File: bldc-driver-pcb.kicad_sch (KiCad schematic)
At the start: 0 parts

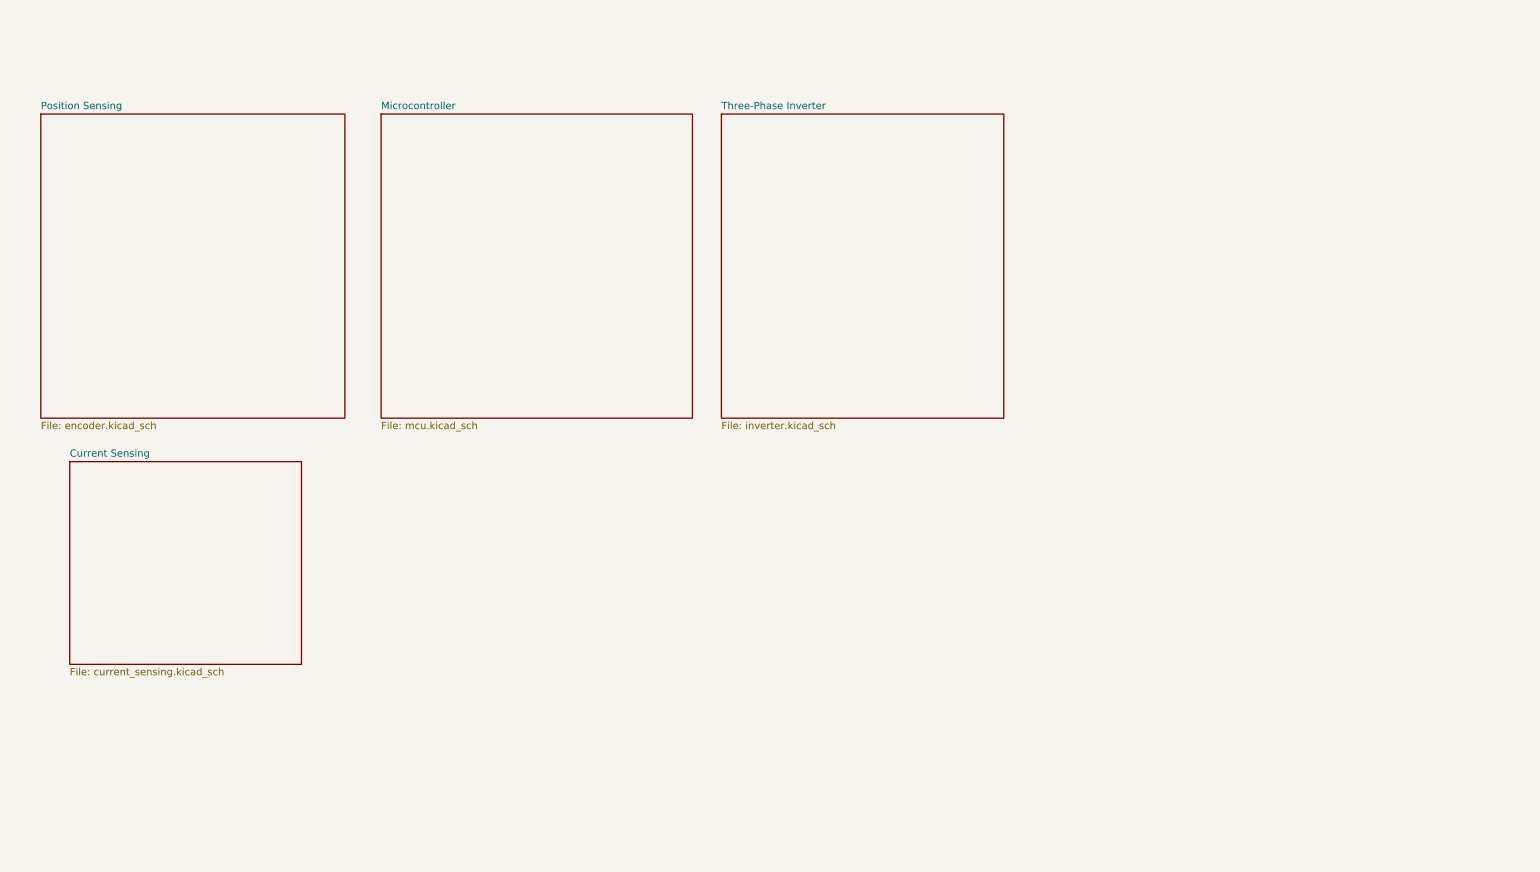
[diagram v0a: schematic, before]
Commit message: Add MCU stuff, cortex debug connector and docs
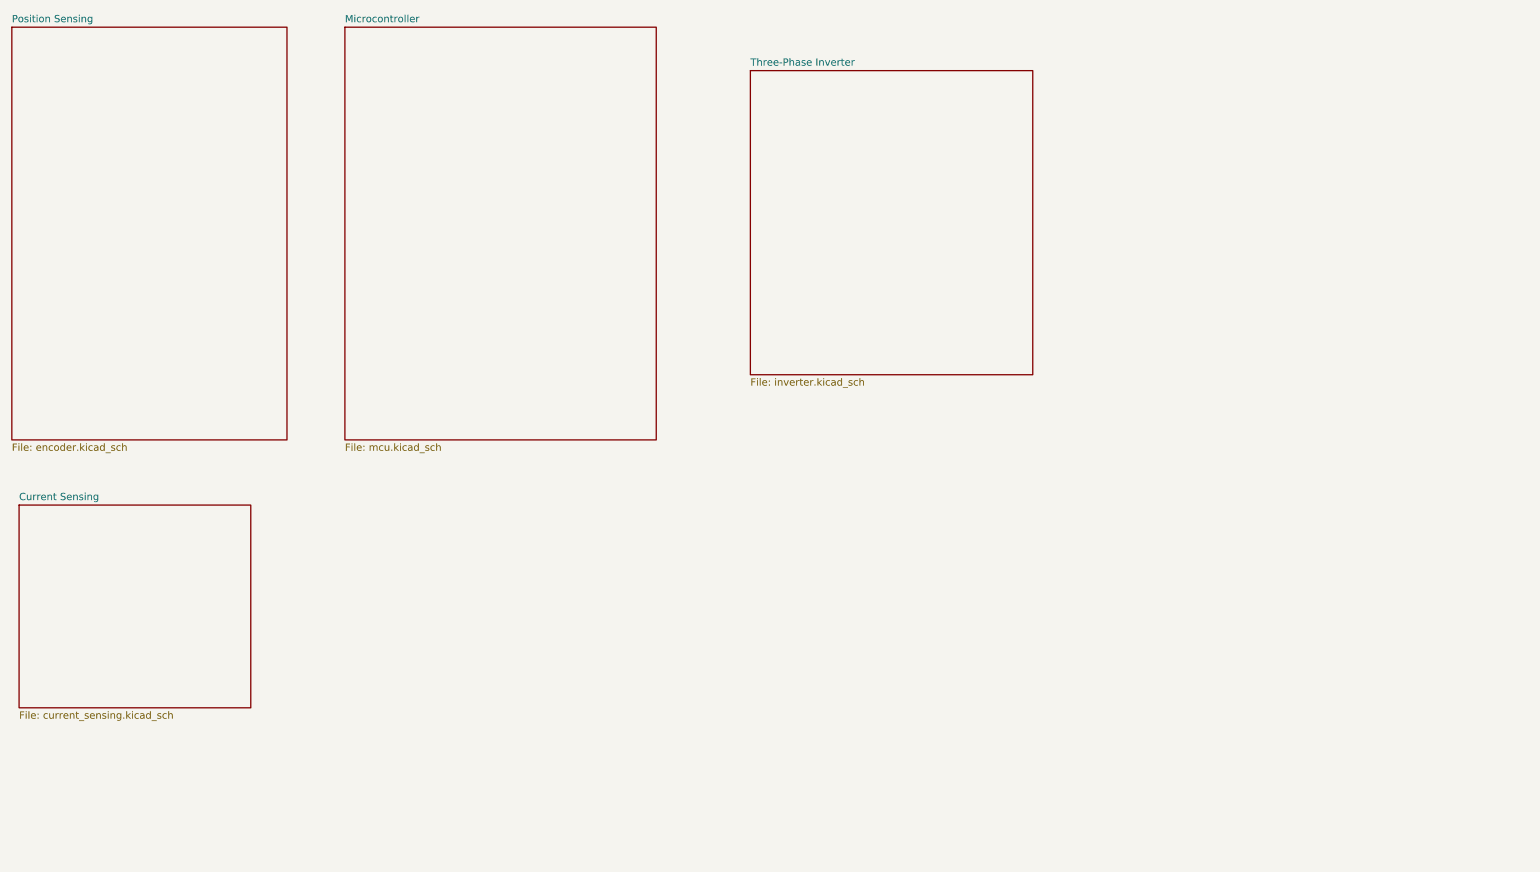
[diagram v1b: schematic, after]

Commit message: Initial routing
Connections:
- no-connect marks 0 -> 9
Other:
- sheet Current Sensing ports: added CSA_1_IN+, CSA_1_IN-, CSA_1_VOUT, CSA_2_IN+, CSA_2_IN-, CSA_2_VOUT, CSA_3_IN+, CSA_3_IN-, CSA_3_VOUT, OPAMP_VCC, VREF_1, VREF_2, VREF_3; removed none
- sheet Microcontroller ports: added 3V3_MCU, ADC_AIN2, ADC_AIN3, ADC_AIN4, ADC_VREFA, ENCODER_CSn, SERCOM1_PAD0, SERCOM1_PAD1, SERCOM1_PAD2, SERCOM1_PAD3, TCC0_WO0, TCC0_WO1, TCC0_WO2, TCC0_WO3, TCC0_WO4, TCC0_WO5, TCC0_WO6, TCC0_WO7; removed none
- sheet Position Sensing ports: added ENCODER_3V3, ENCODER_CSn, ENCODER_MISO, ENCODER_MOSI, ENCODER_SCLK; removed none
- sheet Three-Phase Inverter ports: added CSA_1_IN+, CSA_1_IN-, CSA_2_IN+, CSA_2_IN-, CSA_3_IN+, CSA_3_IN-, HALF_BRIDGE_1_HI, HALF_BRIDGE_1_LO, HALF_BRIDGE_1_OUT, HALF_BRIDGE_2_HI, HALF_BRIDGE_2_LO, HALF_BRIDGE_2_OUT, HALF_BRIDGE_3_HI, HALF_BRIDGE_3_LO, HALF_BRIDGE_3_OUT; removed none

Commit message: More routing
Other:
- sheet Microcontroller ports: added DBG_LED_GREEN, DBG_LED_RED, DRV8316_CSn, RESET, SERCOM3_PAD0, SERCOM3_PAD1, SERCOM5_PAD2, SERCOM5_PAD3, SWCLK, SWDIO, USB_D+, USB_D-, VDDANA, VDDCORE, VDDIN, VDDIO, XIN, XIN32, XOUT, XOUT32; removed none

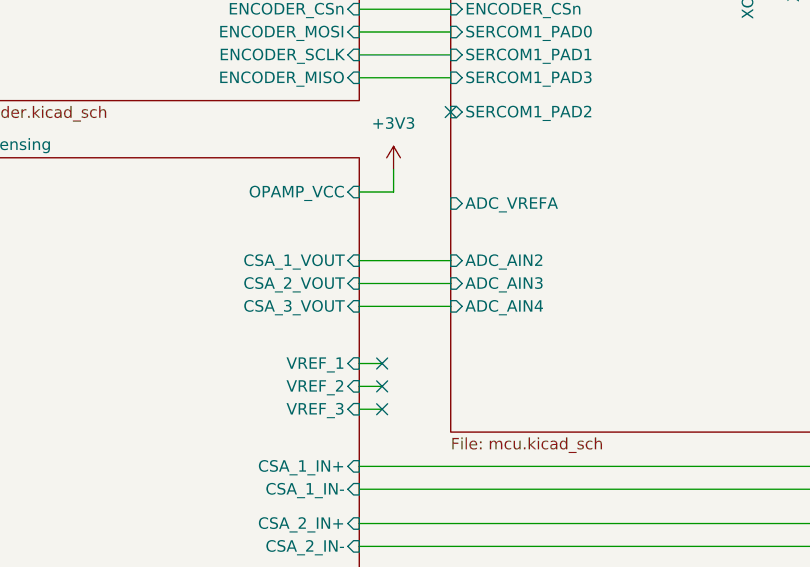
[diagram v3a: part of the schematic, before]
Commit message: Reroute everything
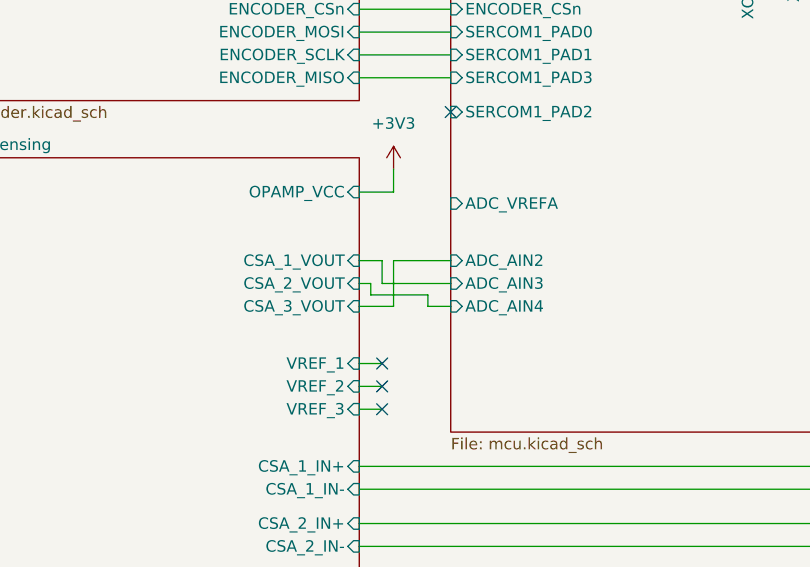
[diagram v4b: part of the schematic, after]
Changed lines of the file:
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@@
+	(wire
+		(pts
+			(xy 102.87 60.96) (xy 105.41 60.96)
+		)
+		(stroke
+			(width 0)
+			(type default)
+		)
+	)
 	(wire
 		(pts
@@
 	(wire
 		(pts
+			(xy 97.79 58.42) (xy 105.41 58.42)
+		)
+		(stroke
+			(width 0)
+			(type default)
+		)
+	)
+	(wire
+		(pts
+			(xy 95.25 58.42) (xy 96.52 58.42)
+		)
+		(stroke
+			(width 0)
+			(type default)
+		)
+	)
+	(wire
+		(pts
 			(xy 99.06 48.26) (xy 99.06 45.72)
 		)
@@
 	(wire
 		(pts
-			(xy 95.25 58.42) (xy 105.41 58.42)
+			(xy 99.06 55.88) (xy 105.41 55.88)
+		)
+		(stroke
+			(width 0)
+			(type default)
+		)
+	)
+	(wire
+		(pts
+			(xy 99.06 60.96) (xy 99.06 55.88)
 		)
 		(stroke
@@
 	(wire
 		(pts
+			(xy 97.79 55.88) (xy 97.79 58.42)
+		)
+		(stroke
+			(width 0)
+			(type default)
+		)
+	)
+	(wire
+		(pts
 			(xy 95.25 93.98) (xy 186.69 93.98)
 		)
@@
 	(wire
 		(pts
+			(xy 95.25 60.96) (xy 99.06 60.96)
+		)
+		(stroke
+			(width 0)
+			(type default)
+		)
+	)
+	(wire
+		(pts
 			(xy 95.25 48.26) (xy 99.06 48.26)
 		)
@@
 	(wire
 		(pts
-			(xy 95.25 55.88) (xy 105.41 55.88)
+			(xy 96.52 58.42) (xy 96.52 59.69)
 		)
 		(stroke
@@
 	(wire
 		(pts
+			(xy 96.52 59.69) (xy 102.87 59.69)
+		)
+		(stroke
+			(width 0)
+			(type default)
+		)
+	)
+	(wire
+		(pts
 			(xy 175.26 44.45) (xy 186.69 44.45)
 		)
@@
 	(wire
 		(pts
-			(xy 95.25 60.96) (xy 105.41 60.96)
-		)
-		(stroke
-			(width 0)
-			(type default)
-		)
-	)
-	(wire
-		(pts
 			(xy 175.26 41.91) (xy 186.69 41.91)
 		)
@@
 	(wire
 		(pts
+			(xy 95.25 55.88) (xy 97.79 55.88)
+		)
+		(stroke
+			(width 0)
+			(type default)
+		)
+	)
+	(wire
+		(pts
 			(xy 175.26 31.75) (xy 186.69 31.75)
 		)
@@
 		)
 		(stroke
+			(width 0)
+			(type default)
+		)
+	)
+	(wire
+		(pts
+			(xy 102.87 59.69) (xy 102.87 60.96)
+		)
+		(stroke

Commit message: Finalize layout -- VREF pending
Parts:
- added J3, J4: 505567-0671, bldc-driver-pcb:5055670671, symbol bldc-driver-pcb:505567-0671
- added J5: 505567-0471, bldc-driver-pcb:5055670471, symbol bldc-driver-pcb:505567-0471
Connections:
- net +3V3: now also J3.6, J4.1
- new net GND: J3.3, J3.5, J4.2, J4.4, J5.3, J5.4
- new net SWCLK: J4.5
- new net SWDIO: J4.6
- new net USART3_Rx: J3.2
- new net USART3_Tx: J3.4
- new net USART5_Tx: J3.1
- new net VBUS: J5.1, J5.2
- new net nRST: J4.3
- no-connect marks 9 -> 16
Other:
- sheet Microcontroller ports: added none; removed DBG_LED_GREEN, DBG_LED_RED, DRV8316_CSn, VDDANA, VDDCORE, VDDIN, VDDIO, XIN, XIN32, XOUT, XOUT32

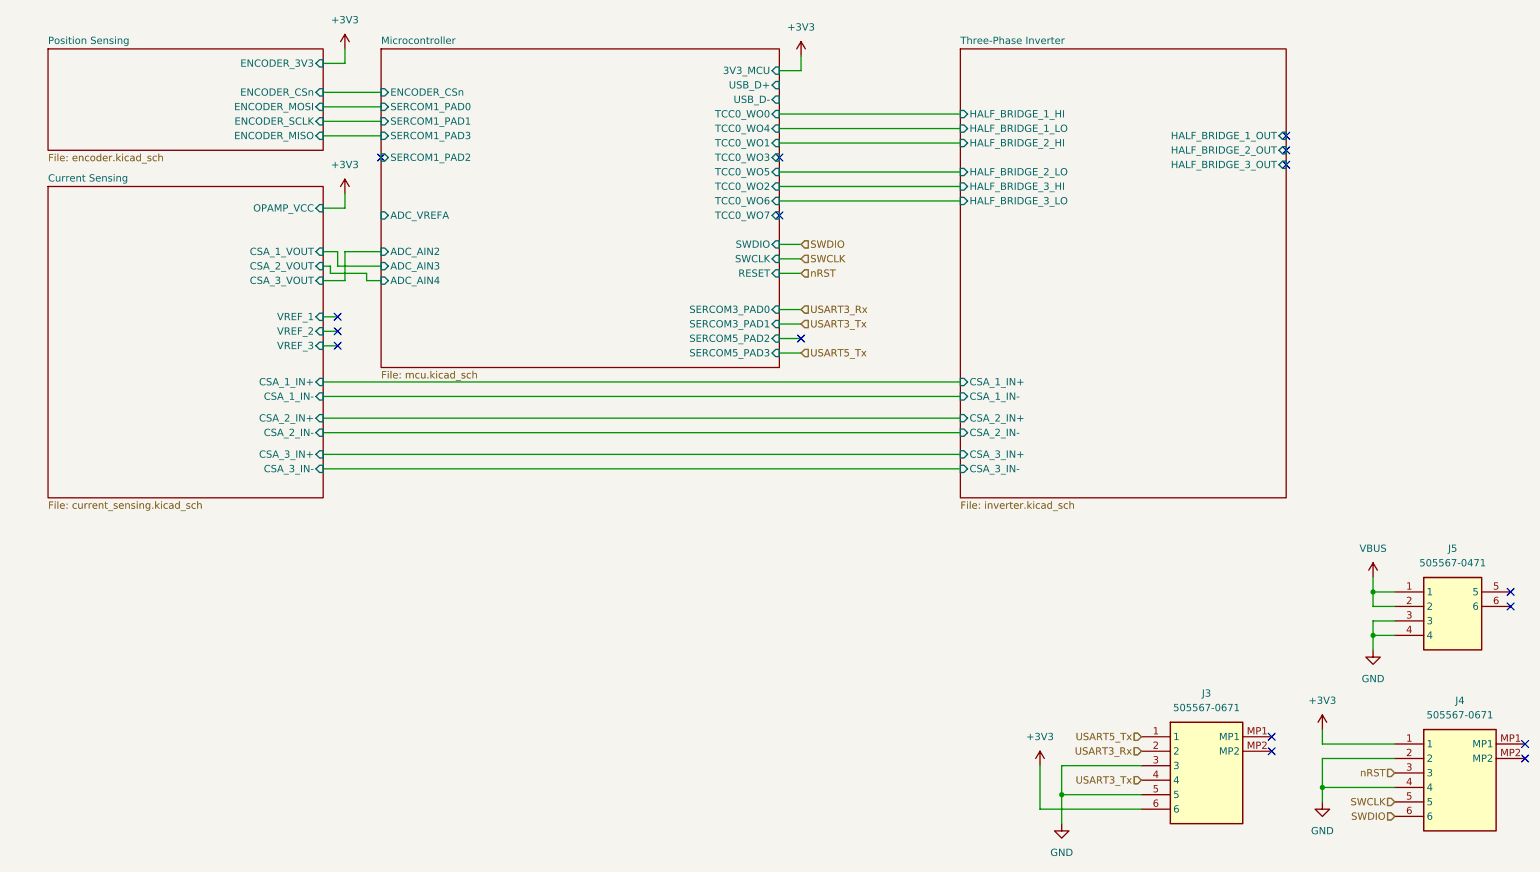
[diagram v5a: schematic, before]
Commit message: Add connector for motor phases
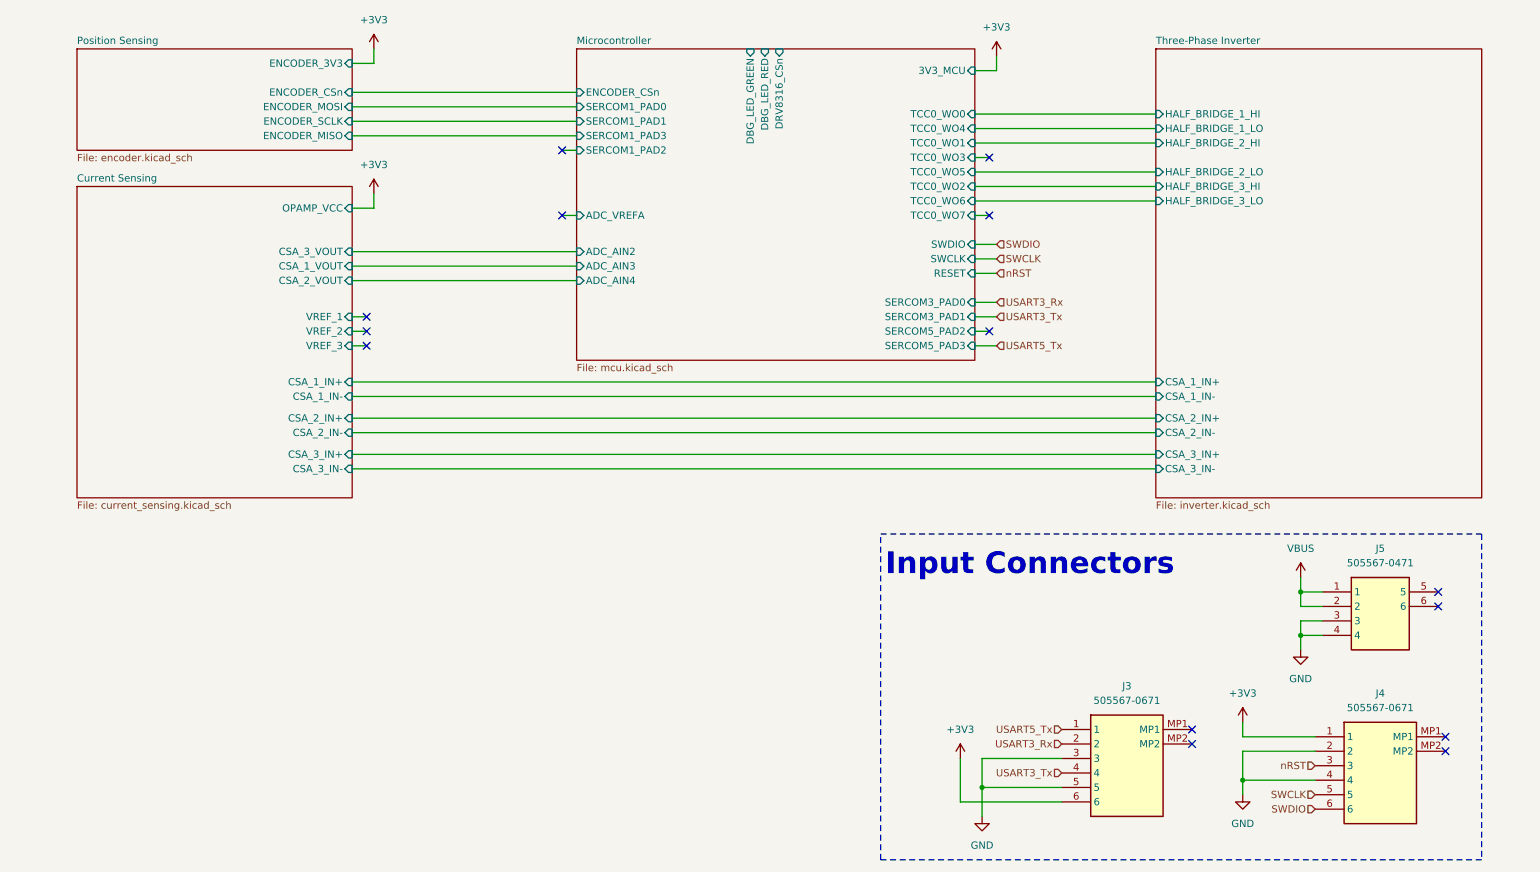
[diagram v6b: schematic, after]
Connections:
- no-connect marks 16 -> 14
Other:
- sheet Microcontroller ports: added DBG_LED_GREEN, DBG_LED_RED, DRV8316_CSn; removed USB_D+, USB_D-
- sheet Three-Phase Inverter ports: added none; removed HALF_BRIDGE_1_OUT, HALF_BRIDGE_2_OUT, HALF_BRIDGE_3_OUT
- note added: "Input Connectors"
- moved on the sheet: J3, J4, J5

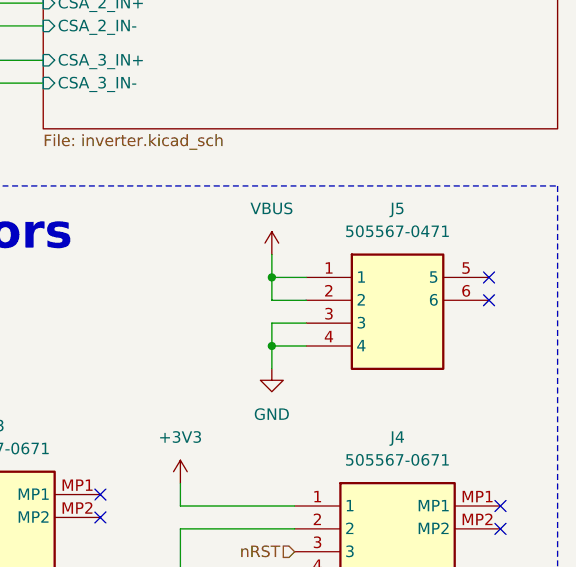
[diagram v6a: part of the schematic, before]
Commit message: Relocate VM & phase connectors
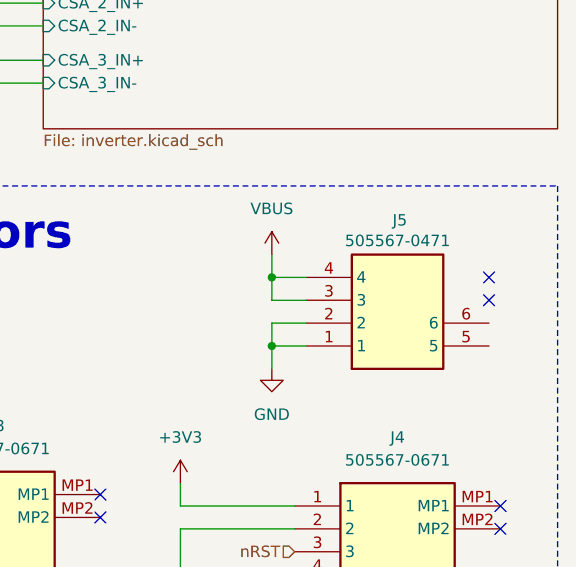
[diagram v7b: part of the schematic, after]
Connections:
- net GND: now also J5.1, J5.2; no longer J5.3, J5.4
- net VBUS: now also J5.3, J5.4; no longer J5.1, J5.2
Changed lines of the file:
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@@
 		(lib_id "bldc-driver-pcb:505567-0471")
 		(at 254 119.38 0)
+		(mirror x)
 		(unit 1)
 		(exclude_from_sim no)
@@
 		(on_board yes)
 		(dnp no)
-		(fields_autoplaced yes)
 		(property "Reference" "J5"
-			(at 254 107.95 0)
+			(at 254.254 109.22 0)
 			(effects
 				(font
@@
 		)
 		(property "Value" "505567-0471"
-			(at 254 110.49 0)
+			(at 254 111.506 0)
 			(effects
 				(font
@@
 		)
 		(property "Footprint" "bldc-driver-pcb:5055670471"
-			(at 270.51 214.3 0)
+			(at 270.51 24.46 0)
 			(effects
 				(font
@@
 		)
 		(property "Datasheet" "http://www.molex.com/webdocs/datasheets/pdf/en-us//5055670471_PCB_HEADERS.pdf"
-			(at 270.51 314.3 0)
+			(at 270.51 -75.54 0)
 			(effects
 				(font
@@
 		)
 		(property "Height" "3"
-			(at 270.51 514.3 0)
+			(at 270.51 -275.54 0)
 			(effects
 				(font
@@
 		)
 		(property "Mouser Part Number" "538-505567-0471"
-			(at 270.51 614.3 0)
+			(at 270.51 -375.54 0)
 			(effects
 				(font
@@
 		)
 		(property "Mouser Price/Stock" "https://www.mouser.co.uk/ProductDetail/Molex/505567-0471?qs=gt1LBUVyoHnKtp3R0Oh0Cg%3D%3D"
-			(at 270.51 714.3 0)
+			(at 270.51 -475.54 0)
 			(effects
 				(font
@@
 		)
 		(property "Manufacturer_Name" "Molex"
-			(at 270.51 814.3 0)
+			(at 270.51 -575.54 0)
 			(effects
 				(font
@@
 		)
 		(property "Manufacturer_Part_Number" "505567-0471"
-			(at 270.51 914.3 0)
+			(at 270.51 -675.54 0)
 			(effects
 				(font
